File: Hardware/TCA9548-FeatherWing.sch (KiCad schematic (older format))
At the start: 44 parts, among them J1 Conn_01x03, J10 JST_SH, J11 Conn_01x16, J12 Conn_01x12, J2 JST_PH-SH, J3 JST_PH-SH, J4 Conn_01x03, J5 JST_SH, J6 JST_SH, J7 JST_SH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

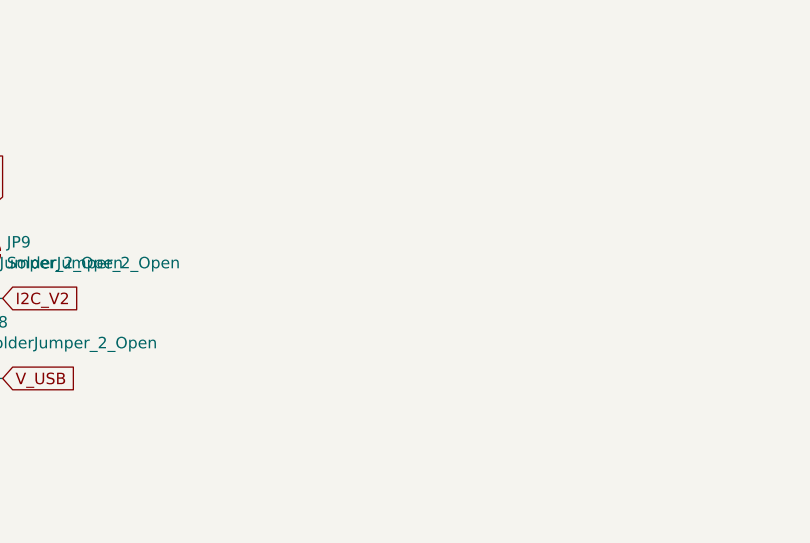
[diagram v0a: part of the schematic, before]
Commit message: Add pullups to source lines
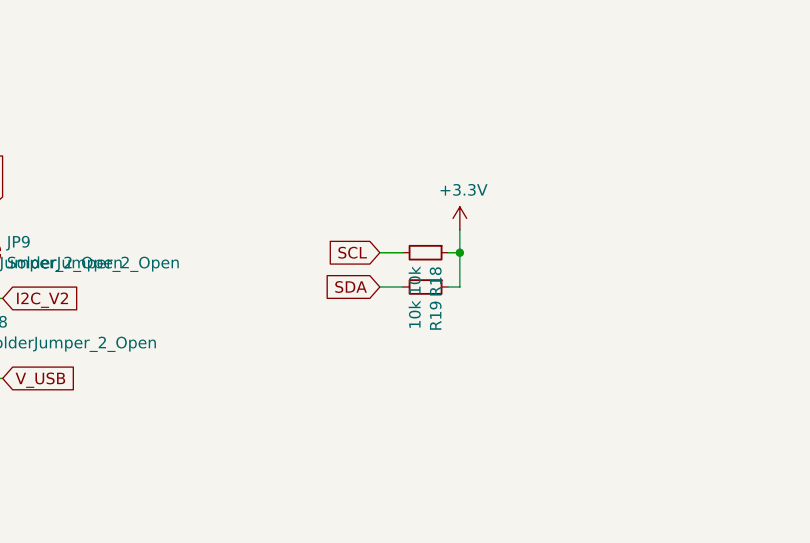
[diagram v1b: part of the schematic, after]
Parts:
- added R18, R19: 10k, digikey-footprints:0805, symbol Device:R_Small
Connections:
- net +3V3: now also R18.1, R19.1
- net SCL: now also R18.2
- net SDA: now also R19.2
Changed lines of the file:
@@
 Wire Wire Line
 	1950 2900 1950 3150
+Text GLabel 6200 1400 0    50   Input ~ 0
+SCL
+Text GLabel 6200 1550 0    50   Input ~ 0
+SDA
+$Comp
+L Device:R_Small R18
+U 1 1 600B170C
+P 6400 1400
+F 0 "R18" H 6459 1446 50  0000 L CNN
+F 1 "10k" H 6459 1355 50  0000 L CNN
+F 2 "digikey-footprints:0805" H 6400 1400 50  0001 C CNN
+F 3 "~" H 6400 1400 50  0001 C CNN
+	1    6400 1400
+	0    1    1    0
+$EndComp
+$Comp
+L Device:R_Small R19
+U 1 1 600B1FAB
+P 6400 1550
+F 0 "R19" H 6459 1596 50  0000 L CNN
+F 1 "10k" H 6459 1505 50  0000 L CNN
+F 2 "digikey-footprints:0805" H 6400 1550 50  0001 C CNN
+F 3 "~" H 6400 1550 50  0001 C CNN
+	1    6400 1550
+	0    1    1    0
+$EndComp
+$Comp
+L power:+3.3V #PWR0101
+U 1 1 600B2190
+P 6550 1300
+F 0 "#PWR0101" H 6550 1150 50  0001 C CNN
+F 1 "+3.3V" H 6565 1473 50  0000 C CNN
+F 2 "" H 6550 1300 50  0001 C CNN
+F 3 "" H 6550 1300 50  0001 C CNN
+	1    6550 1300
+	1    0    0    -1
+$EndComp
+Wire Wire Line
+	6200 1400 6300 1400
+Wire Wire Line
+	6200 1550 6300 1550
+Wire Wire Line
+	6500 1550 6550 1550
+Wire Wire Line
+	6550 1550 6550 1400
+Wire Wire Line
+	6500 1400 6550 1400
+Connection ~ 6550 1400
+Wire Wire Line
+	6550 1400 6550 1300
 $EndSCHEMATC
